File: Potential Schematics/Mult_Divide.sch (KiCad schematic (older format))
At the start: 1 part

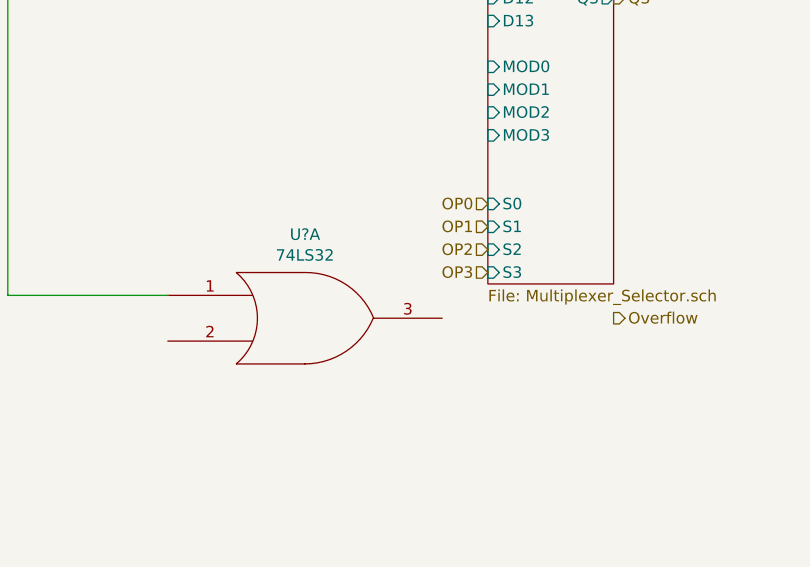
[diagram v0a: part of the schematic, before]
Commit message: Updated overview of Schematic
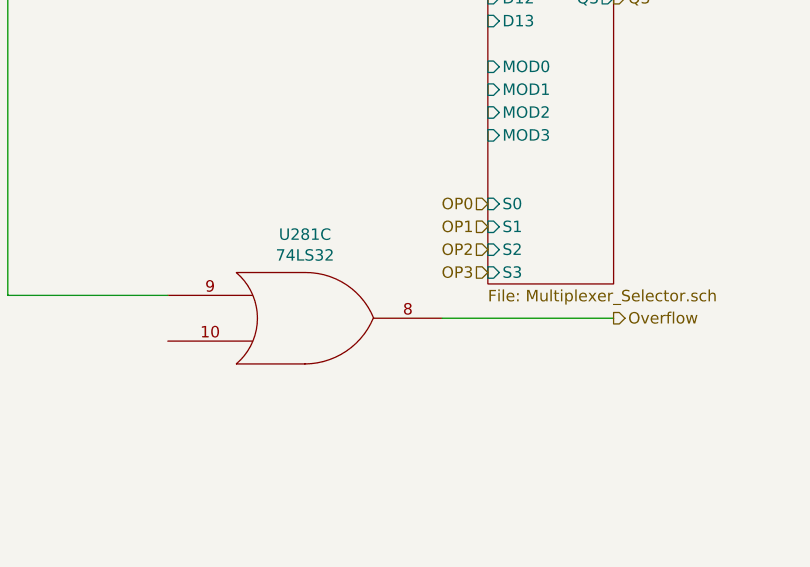
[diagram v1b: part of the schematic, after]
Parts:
- gave numbers to parts that had none: 1
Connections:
- net Multiplier/Overflow: now also U281.9; no longer U281.1
- net Overflow: now also U281.8
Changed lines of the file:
@@
 $Descr A4 11693 8268
 encoding utf-8
-Sheet 450 467
+Sheet 450 902
 Title ""
 Date ""
@@
 	1800 1050 4200 1050
 $Comp
-L 4-bit_processor-rescue:74LS32 U?
-U 1 1 5BB645F8
+L 4-bit_processor-rescue:74LS32 U281
+U 3 1 5BB645F8
 P 7900 5550
-F 0 "U?" H 7900 5916 50  0000 C CNN
+F 0 "U281" H 7900 5916 50  0000 C CNN
 F 1 "74LS32" H 7900 5825 50  0000 C CNN
 F 2 "" H 7900 5550 50  0001 C CNN
 F 3 "" H 7900 5550 50  0001 C CNN
-	1    7900 5550
+	3    7900 5550
 	1    0    0    -1
 $EndComp
@@
 Wire Wire Line
 	6600 5450 6600 1350
+Wire Wire Line
+	8500 5550 9250 5550
 $EndSCHEMATC
